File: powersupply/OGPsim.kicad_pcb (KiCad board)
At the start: 4 copper layers, 31 parts, among them Q1 Q_NPN_BEC, Q2 Q_NPN_BEC, Q5 Q_NPN_BEC, U1 LM317_TO39

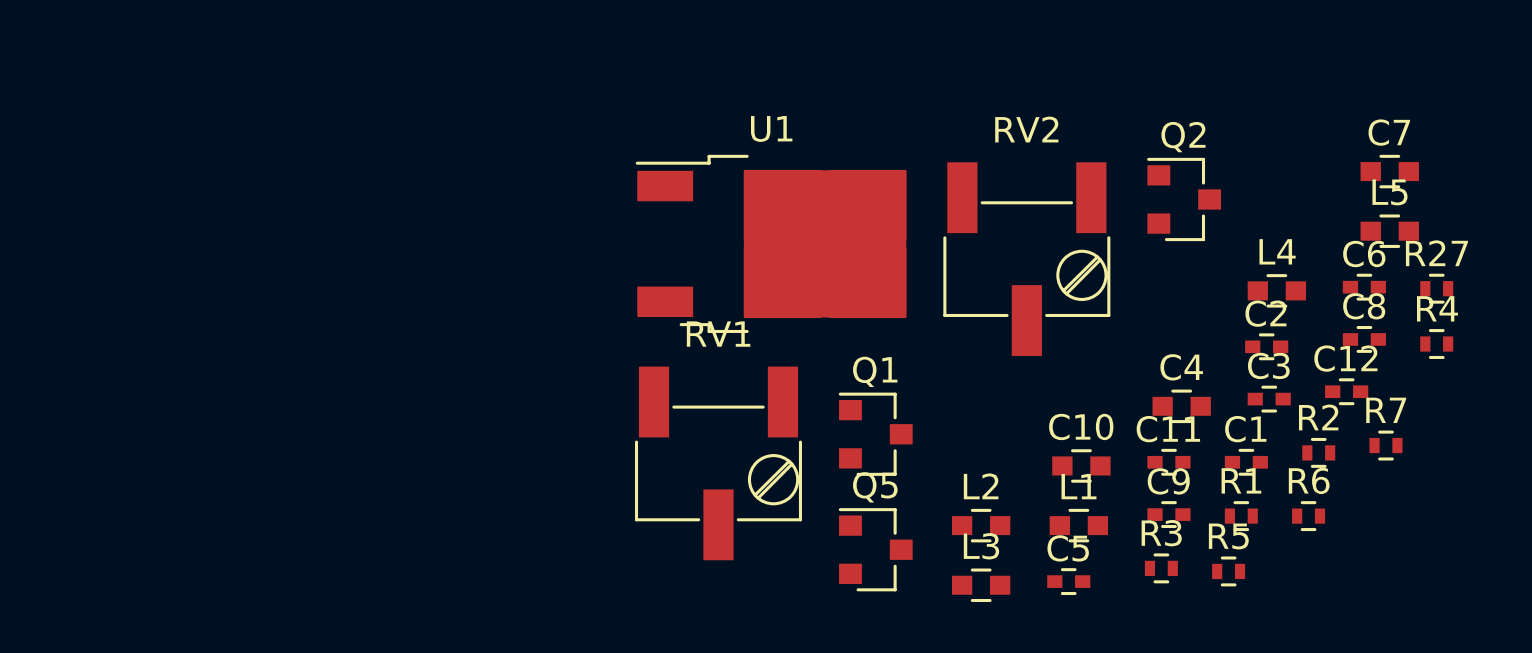
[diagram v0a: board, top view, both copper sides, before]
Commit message: Updated power supply board layout.
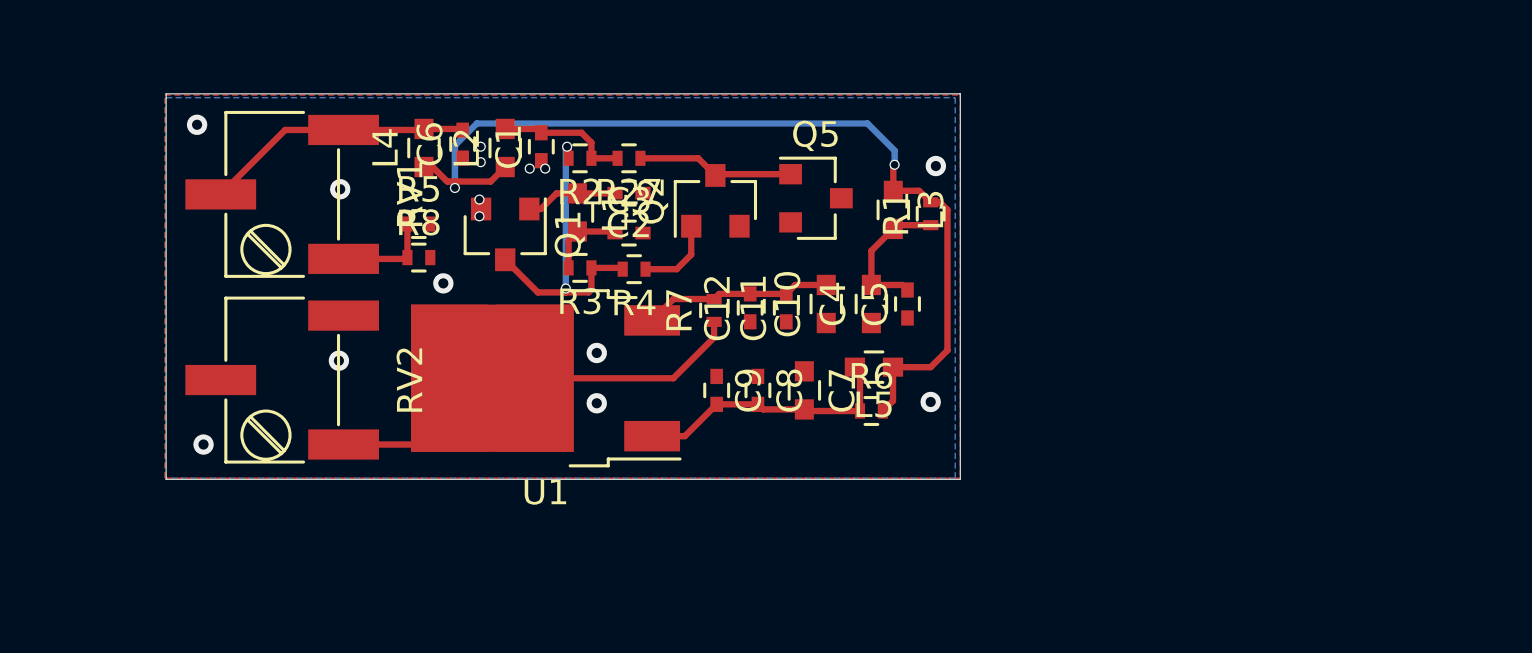
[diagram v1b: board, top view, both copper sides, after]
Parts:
- added R8: 200, Resistors_SMD:R_0402, F.Cu at (146.2, 93.1)
- moved C6 36.0 mm to (147.9, 88.6), turned to 90 degrees
- moved R5 34.7 mm to (146.2, 91.8)
- moved L4 34.1 mm to (146.4, 88.8), turned to 90 degrees
- moved R27 32.2 mm to (154.4, 89.2), turned to 180 degrees
- moved R4 31.8 mm to (154.6, 93.6), turned to 180 degrees
- moved R2 31.3 mm to (152.5, 89.2), turned to 180 degrees
- moved C1 30.4 mm to (151.0, 88.7), turned to 90 degrees
- moved RV2 29.7 mm to (140.8, 97.9), turned to 270 degrees
- moved R7 27.0 mm to (157.8, 95.2), turned to 90 degrees
- moved C3 26.1 mm to (154.4, 92.2)
- moved C2 25.8 mm to (154.4, 90.6), turned to 180 degrees
- moved R3 25.8 mm to (152.5, 93.5), turned to 180 degrees
- moved C7 24.6 mm to (161.3, 98.3), turned to 270 degrees
- moved C8 24.0 mm to (159.5, 98.3), turned to 270 degrees
- moved L2 23.9 mm to (149.6, 88.8), turned to 90 degrees
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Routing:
- net +BATT: track 0.00 -> 37.6 mm, vias 0 -> 2
- net Net-(R7-Pad1): track 0.00 -> 17.0 mm
- net Net-(Q1-Pad3): track 0.00 -> 12.3 mm, vias 0 -> 2
- net Net-(C7-Pad2): track 0.00 -> 10.6 mm
- net Net-(C6-Pad2): track 0.00 -> 10.6 mm
- net +4V: track 0.00 -> 7.44 mm
- net Net-(Q2-Pad3): track 0.00 -> 6.22 mm
- net +9V: track 0.00 -> 5.61 mm
- net Net-(C1-Pad2): track 0.00 -> 5.27 mm
- net Net-(R5-Pad1): track 0.00 -> 3.86 mm
- net Net-(C2-Pad2): track 0.00 -> 3.64 mm
- net Net-(Q2-Pad1): track 0.00 -> 3.16 mm
- net Net-(C3-Pad1): track 0.00 -> 3.09 mm
- net GND: vias 0 -> 15
- added copper zone on B.Cu, net GND
- added copper zone on F.Cu, net GND
- removed copper zone on In1.Cu, net (none)
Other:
- board outline added: 31.3 x 15.2 mm
- copper layers 4 -> 2

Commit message: Updated power supply board and schematic to have solderable pads.
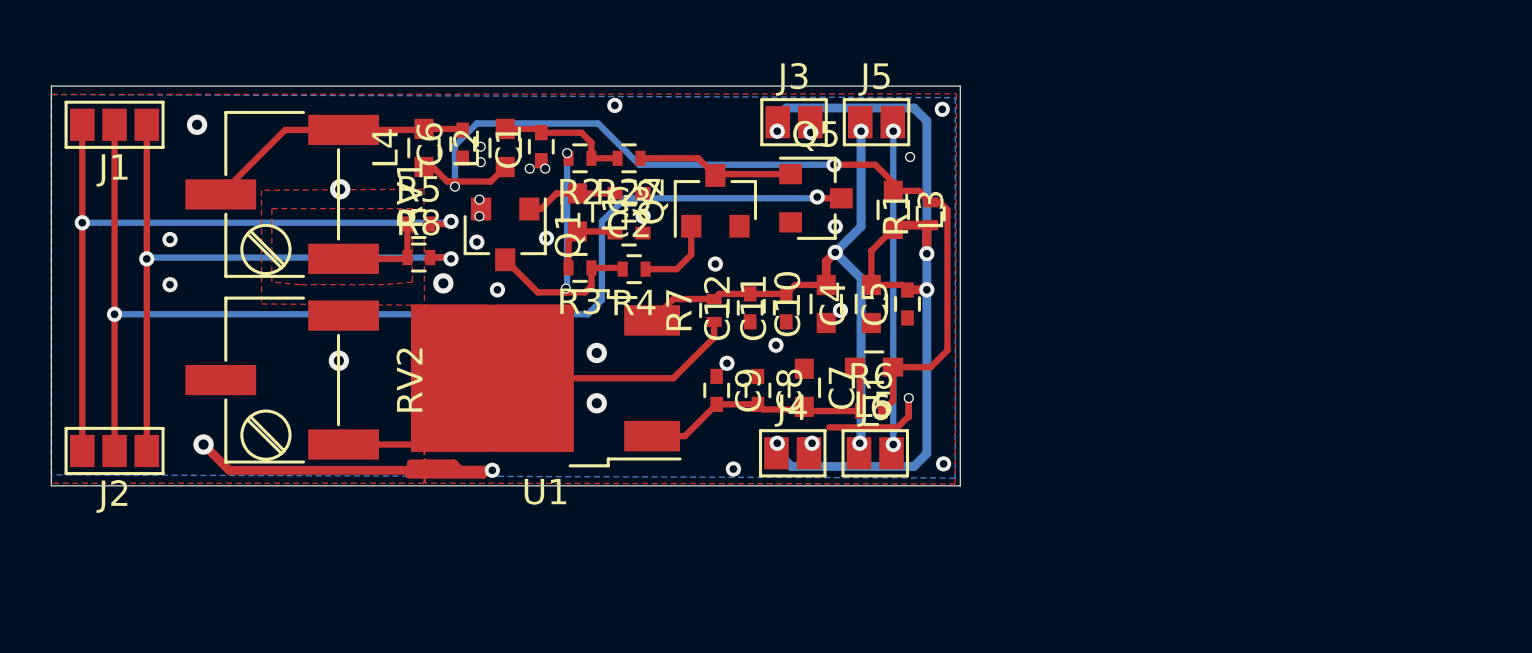
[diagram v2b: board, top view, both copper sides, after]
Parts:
- added J1: Conn_01x03, Connect:GS3, F.Cu at (134.2, 87.9)
- added J2: Conn_01x03, Connect:GS3, F.Cu at (134.2, 100.7)
- added J3: Conn_01x02, Connect:GS2, F.Cu at (160.9, 87.8)
- added J4: Conn_01x02, Connect:GS2, F.Cu at (160.9, 100.8)
- added J5: Conn_01x02, Connect:GS2, F.Cu at (164.2, 87.8)
- added J6: Conn_01x02, Connect:GS2, F.Cu at (164.1, 100.8)
- moved C7 0.10 mm to (161.3, 98.2)
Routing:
- net Net-(J1-Pad2): track 0.00 -> 45.2 mm, vias 0 -> 2
- net +9V: track 5.61 -> 34.2 mm, vias 0 -> 4
- net Net-(J1-Pad1): track 0.00 -> 28.2 mm, vias 0 -> 2
- net Net-(J1-Pad3): track 0.00 -> 25.7 mm, vias 0 -> 2
- net GND: track 0.00 -> 23.3 mm, vias 15 -> 33
- net +4V: track 7.44 -> 22.0 mm, vias 0 -> 3
- net Net-(J5-Pad2): track 0.00 -> 12.3 mm, vias 0 -> 2
- net Net-(Q1-Pad3): track 12.3 -> 11.5 mm
- net +BATT: track 37.6 -> 36.8 mm
- added copper zone on F.Cu, net Net-(R5-Pad1)
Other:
- board size 31.3 x 15.2 mm -> 35.8 x 15.7 mm

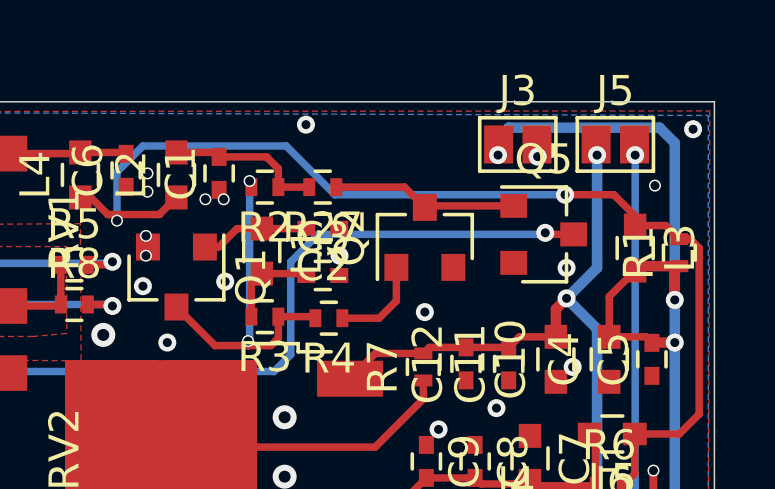
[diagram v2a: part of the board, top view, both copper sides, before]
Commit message: Added TODO list. Added solder pads for power input on power supply board.
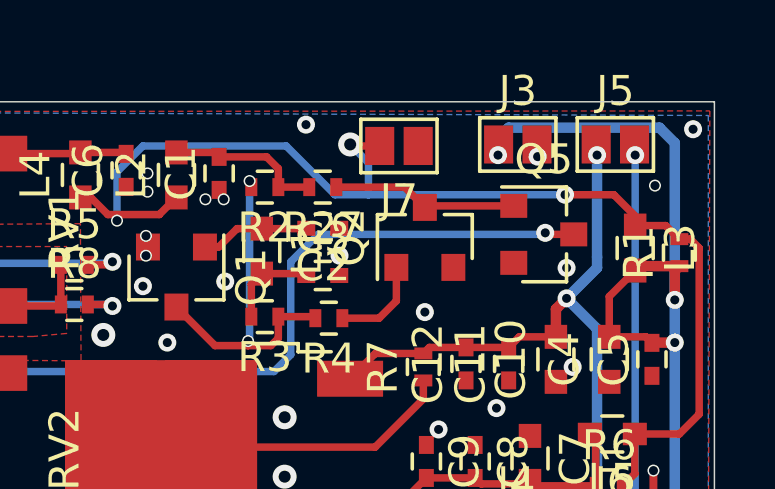
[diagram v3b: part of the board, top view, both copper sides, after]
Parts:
- added J7: Conn_01x02, Connect:GS2, F.Cu at (157.0, 87.8)
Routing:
- net +BATT: track 36.8 -> 39.7 mm, vias 2 -> 3

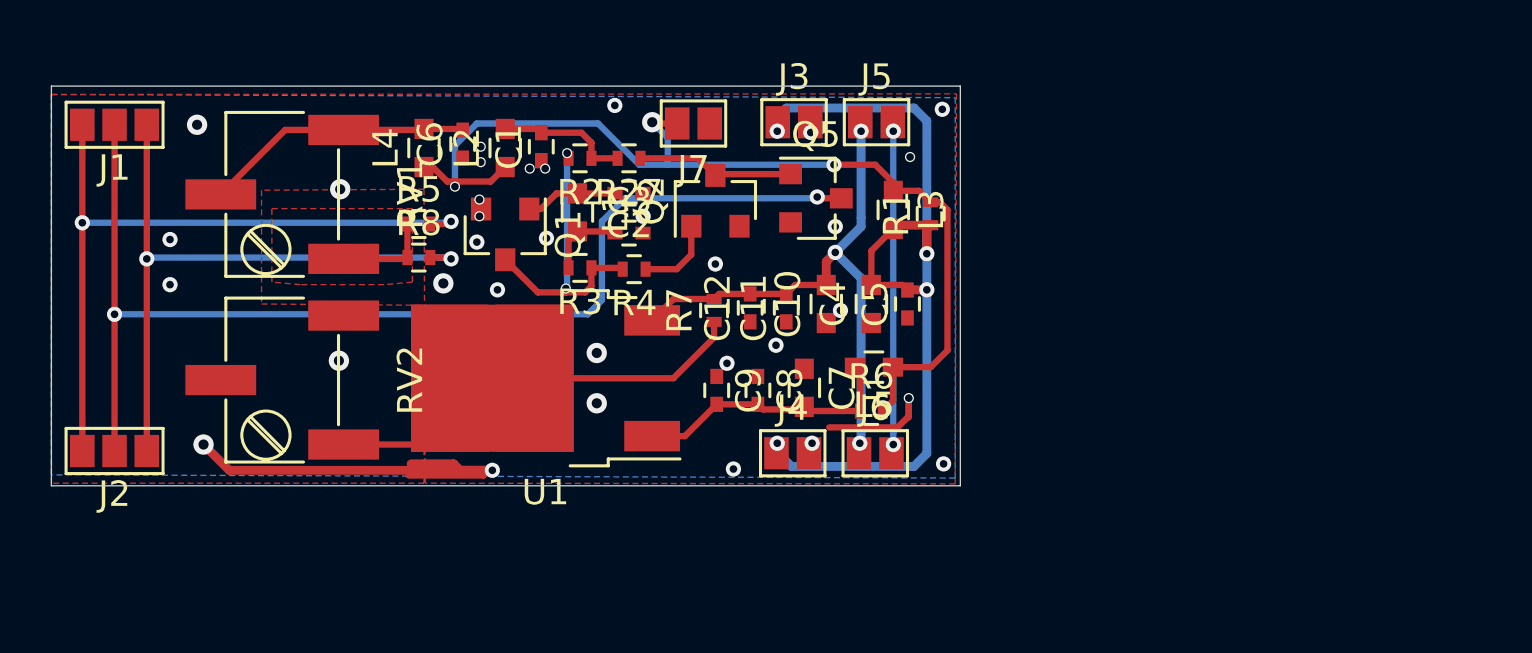
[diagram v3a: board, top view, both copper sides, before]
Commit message: Cleaned up silk screen layers and moved part REFs to UserDrawings. Made PNG image file of part REFs for Power Supply and Pickup Boards.
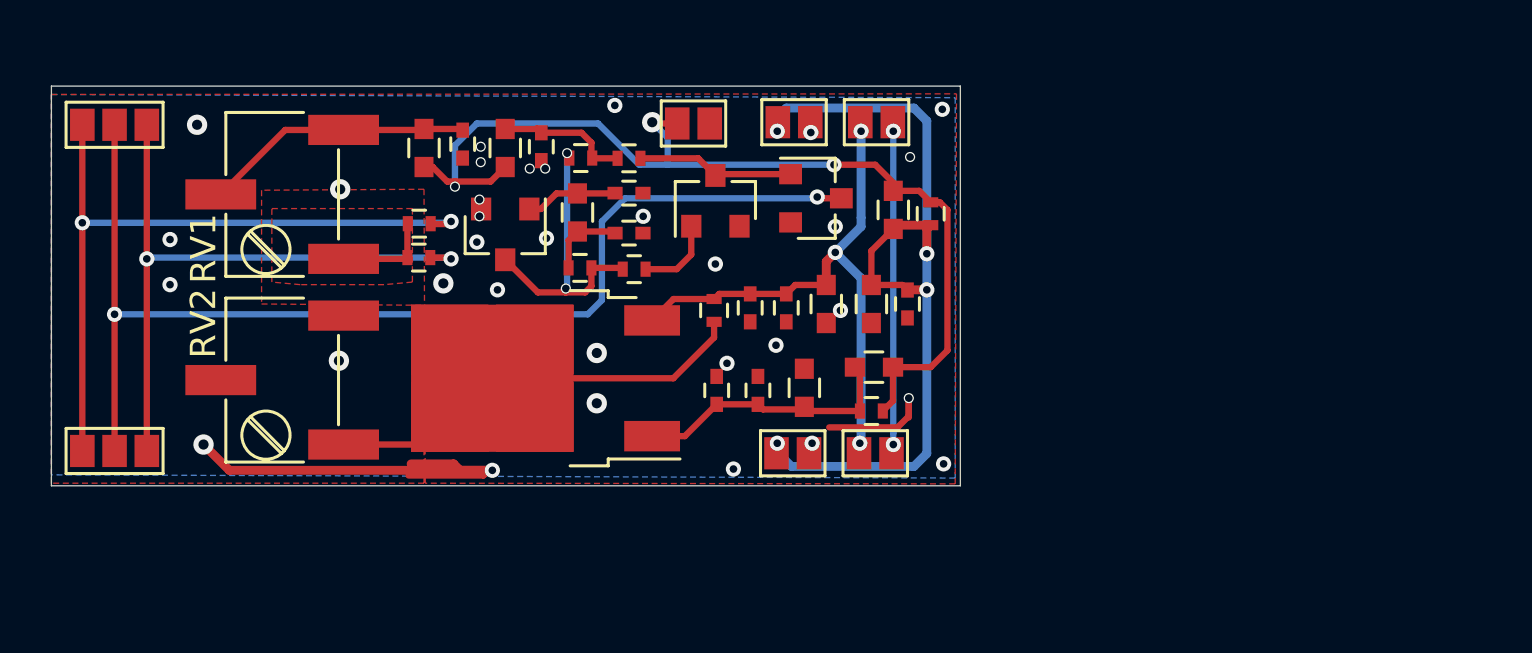
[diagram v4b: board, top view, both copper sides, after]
